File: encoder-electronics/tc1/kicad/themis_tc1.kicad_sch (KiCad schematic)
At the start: 69 parts, among them J1 Screw_Terminal_01x03, J10 Conn_01x02_Pin, J2 Conn_01x06_Pin, J3 Screw_Terminal_01x02, J4 Conn_01x02_Pin, J5 Conn_01x02_Pin, J6 Screw_Terminal_01x02, J7 Conn_01x02_Pin, J8 Conn_01x02_Pin, J9 Conn_01x02_Pin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

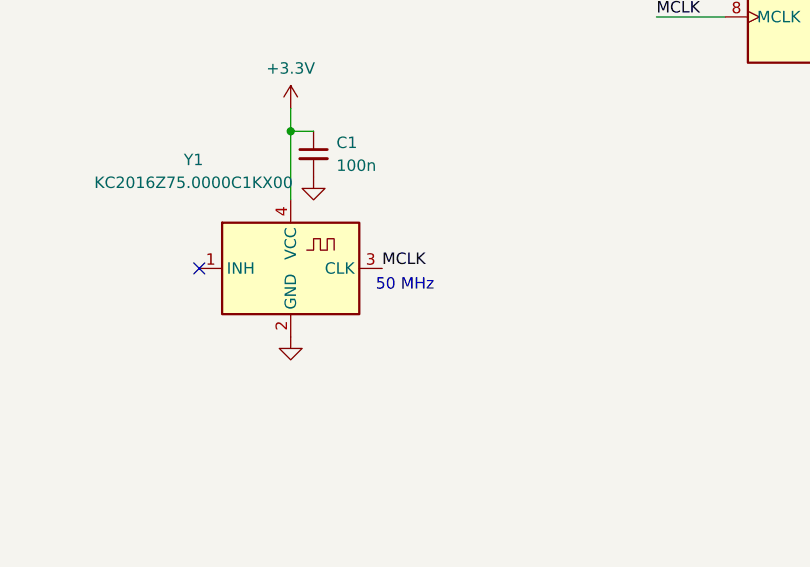
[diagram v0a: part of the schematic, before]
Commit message: TC1 bringup: AD9834 DDS producing 1 MHz sine wave
- Fix MCLK_HZ: oscillator is 75 MHz (BOM was correct, schematic was wrong)
- Fix root cause of silent DDS: RESET pin was floating, holding chip in
  reset. Drive RESET LOW before initialising DDS, and construct AD9834
  object inside setup() so SPI is ready.
- Add teensy-cli upload protocol to platformio.ini
- Add AD9834 Arduino library (modified from AliBarber/AD9834)
- Add AD9834 datasheet
- Add notes/AD9834.md with register map, SPI notes, and lessons learned
- Update project notebook with bringup session
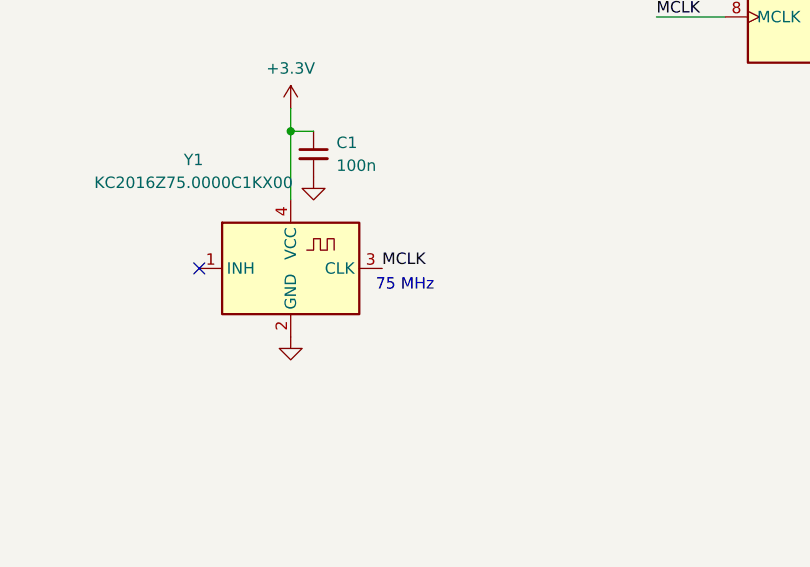
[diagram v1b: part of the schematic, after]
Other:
- note added: "75 MHz"
- note removed: "50 MHz"
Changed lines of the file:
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@@
 		)
 	)
-	(text "50 MHz"
+	(text "75 MHz"
 		(exclude_from_sim no)
 		(at 106.68 260.985 0)
